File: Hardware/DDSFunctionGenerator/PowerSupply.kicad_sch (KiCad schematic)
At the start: 9 parts, among them J4 Conn_01x02_Female, U2 L78L08_SOT89, U3 L78L33_SO8

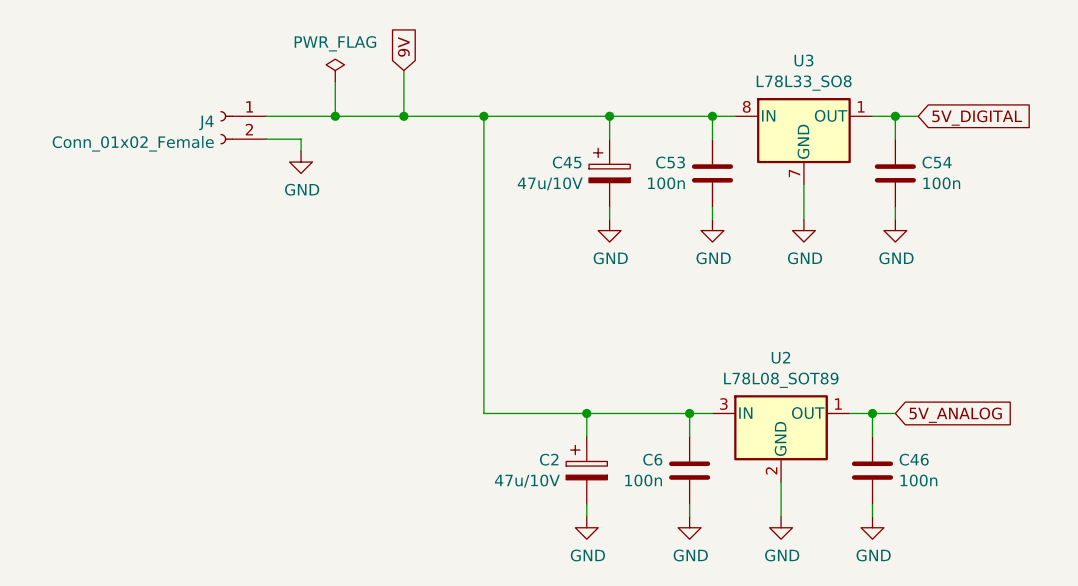
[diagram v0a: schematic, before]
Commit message: move to raspbbery pico, first draft
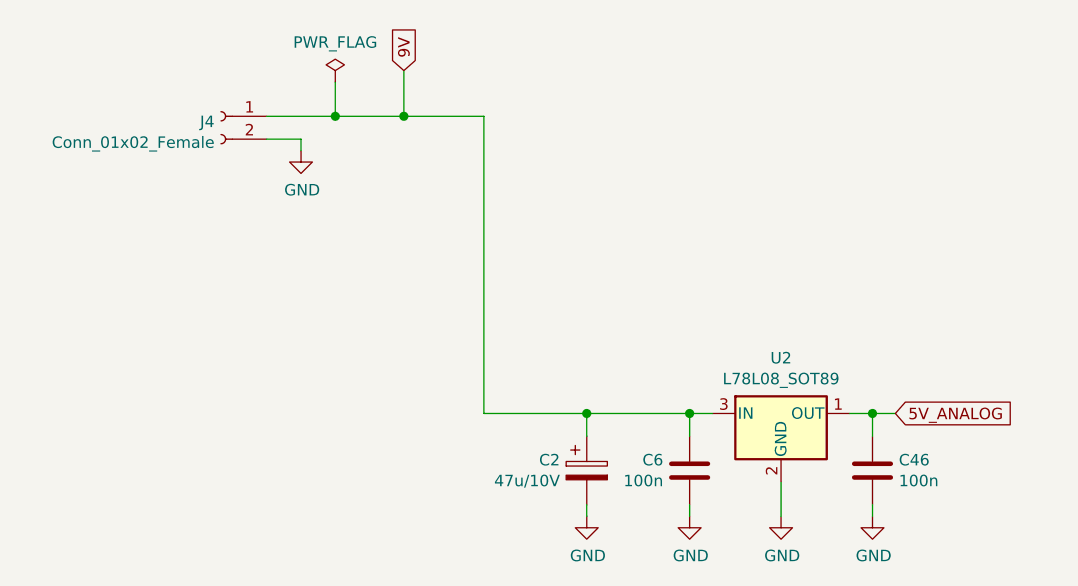
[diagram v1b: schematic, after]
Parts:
- removed C45: 47u/10V, Capacitor_Tantalum_SMD:CP_EIA-3528-21_Kemet-B, symbol Device:CP
- removed C53, C54: 100n, Capacitor_SMD:C_0402_1005Metric, symbol Device:C
- removed U3: L78L33_SO8, Package_SO:SOIC-8_3.9x4.9mm_P1.27mm, symbol DDSFunctionGenerator-rescue:L78L33_SO8-Regulator_Linear
